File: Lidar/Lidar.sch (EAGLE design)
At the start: 4 parts

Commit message: board schematic
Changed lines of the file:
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@@
 <grid distance="0.1" unitdist="inch" unit="inch" style="lines" multiple="1" display="no" altdistance="0.01" altunitdist="inch" altunit="inch"/>
 <layers>
-<layer number="1" name="Top" color="4" fill="1" visible="yes" active="no"/>
-<layer number="16" name="Bottom" color="1" fill="1" visible="yes" active="no"/>
-<layer number="17" name="Pads" color="2" fill="1" visible="yes" active="no"/>
-<layer number="18" name="Vias" color="2" fill="1" visible="yes" active="no"/>
-<layer number="19" name="Unrouted" color="6" fill="1" visible="yes" active="no"/>
-<layer number="20" name="Dimension" color="15" fill="1" visible="yes" active="no"/>
-<layer number="21" name="tPlace" color="7" fill="1" visible="yes" active="no"/>
-<layer number="22" name="bPlace" color="7" fill="1" visible="yes" active="no"/>
-<layer number="23" name="tOrigins" color="15" fill="1" visible="yes" active="no"/>
-<layer number="24" name="bOrigins" color="15" fill="1" visible="yes" active="no"/>
-<layer number="25" name="tNames" color="7" fill="1" visible="yes" active="no"/>
-<layer number="26" name="bNames" color="7" fill="1" visible="yes" active="no"/>
-<layer number="27" name="tValues" color="7" fill="1" visible="yes" active="no"/>
-<layer number="28" name="bValues" color="7" fill="1" visible="yes" active="no"/>
+<layer number="1" name="Top" color="4" fill="1" visible="no" active="no"/>
+<layer number="16" name="Bottom" color="1" fill="1" visible="no" active="no"/>
+<layer number="17" name="Pads" color="2" fill="1" visible="no" active="no"/>
+<layer number="18" name="Vias" color="2" fill="1" visible="no" active="no"/>
+<layer number="19" name="Unrouted" color="6" fill="1" visible="no" active="no"/>
+<layer number="20" name="Dimension" color="15" fill="1" visible="no" active="no"/>
+<layer number="21" name="tPlace" color="7" fill="1" visible="no" active="no"/>
+<layer number="22" name="bPlace" color="7" fill="1" visible="no" active="no"/>
+<layer number="23" name="tOrigins" color="15" fill="1" visible="no" active="no"/>
+<layer number="24" name="bOrigins" color="15" fill="1" visible="no" active="no"/>
+<layer number="25" name="tNames" color="7" fill="1" visible="no" active="no"/>
+<layer number="26" name="bNames" color="7" fill="1" visible="no" active="no"/>
+<layer number="27" name="tValues" color="7" fill="1" visible="no" active="no"/>
+<layer number="28" name="bValues" color="7" fill="1" visible="no" active="no"/>
 <layer number="29" name="tStop" color="7" fill="3" visible="no" active="no"/>
 <layer number="30" name="bStop" color="7" fill="6" visible="no" active="no"/>
@@
 <layer number="35" name="tGlue" color="7" fill="4" visible="no" active="no"/>
 <layer number="36" name="bGlue" color="7" fill="5" visible="no" active="no"/>
-<layer number="37" name="tTest" color="7" fill="1" visible="yes" active="no"/>
-<layer number="38" name="bTest" color="7" fill="1" visible="yes" active="no"/>
+<layer number="37" name="tTest" color="7" fill="1" visible="no" active="no"/>
+<layer number="38" name="bTest" color="7" fill="1" visible="no" active="no"/>
 <layer number="39" name="tKeepout" color="4" fill="11" visible="no" active="no"/>
 <layer number="40" name="bKeepout" color="1" fill="11" visible="no" active="no"/>
@@
 <layer number="44" name="Drills" color="7" fill="1" visible="no" active="no"/>
 <layer number="45" name="Holes" color="7" fill="1" visible="no" active="no"/>
-<layer number="46" name="Milling" color="3" fill="1" visible="yes" active="no"/>
-<layer number="47" name="Measures" color="7" fill="1" visible="yes" active="no"/>
-<layer number="48" name="Document" color="7" fill="1" visible="yes" active="no"/>
-<layer number="49" name="Reference" color="7" fill="1" visible="yes" active="no"/>
-<layer number="50" name="dxf" color="7" fill="1" visible="yes" active="no"/>
-<layer number="51" name="tDocu" color="7" fill="1" visible="yes" active="no"/>
-<layer number="52" name="bDocu" color="7" fill="1" visible="yes" active="no"/>
-<layer number="53" name="tGND_GNDA" color="7" fill="9" visible="yes" active="no"/>
-<layer number="54" name="bGND_GNDA" color="1" fill="9" visible="yes" active="no"/>
-<layer number="56" name="wert" color="7" fill="1" visible="yes" active="no"/>
-<layer number="57" name="tCAD" color="7" fill="1" visible="yes" active="no"/>
-<layer number="58" name="bCAD" color="7" fill="1" visible="yes" active="no"/>
-<layer number="59" name="tCarbon" color="7" fill="1" visible="yes" active="no"/>
-<layer number="60" name="bCarbon" color="7" fill="1" visible="yes" active="no"/>
+<layer number="46" name="Milling" color="3" fill="1" visible="no" active="no"/>
+<layer number="47" name="Measures" color="7" fill="1" visible="no" active="no"/>
+<layer number="48" name="Document" color="7" fill="1" visible="no" active="no"/>
+<layer number="49" name="Reference" color="7" fill="1" visible="no" active="no"/>
+<layer number="50" name="dxf" color="7" fill="1" visible="no" active="no"/>
+<layer number="51" name="tDocu" color="7" fill="1" visible="no" active="no"/>
+<layer number="52" name="bDocu" color="7" fill="1" visible="no" active="no"/>
+<layer number="53" name="tGND_GNDA" color="7" fill="9" visible="no" active="no"/>
+<layer number="54" name="bGND_GNDA" color="1" fill="9" visible="no" active="no"/>
+<layer number="56" name="wert" color="7" fill="1" visible="no" active="no"/>
+<layer number="57" name="tCAD" color="7" fill="1" visible="no" active="no"/>
+<layer number="58" name="bCAD" color="7" fill="1" visible="no" active="no"/>
+<layer number="59" name="tCarbon" color="7" fill="1" visible="no" active="no"/>
+<layer number="60" name="bCarbon" color="7" fill="1" visible="no" active="no"/>
 <layer number="88" name="SimResults" color="9" fill="1" visible="yes" active="yes"/>
 <layer number="89" name="SimProbes" color="9" fill="1" visible="yes" active="yes"/>
@@
 </variantdefs>
 <classes>
-<class number="0" name="default" width="0" drill="0">
+<class number="0" name="default" width="0.8128" drill="0.1016">
+<clearance class="0" value="0.1016"/>
 </class>
 </classes>
@@
 <part name="CONN-LIDAR" library="SparkFun-Connectors" library_urn="urn:adsk.eagle:library:513" deviceset="CONN_05" device="PTH" package3d_urn="urn:adsk.eagle:package:38104/2"/>
 <part name="ESP32" library="ESP32-DEVKITC-32D" deviceset="ESP32-DEVKITC-32D" device=""/>
+<part name="GND1" library="supply1" library_urn="urn:adsk.eagle:library:371" deviceset="GND" device=""/>
 </parts>
 <sheets>
@@
 <attribute name="NAME" x="48.2428" y="104.8043" size="1.78" layer="95"/>
 <attribute name="VALUE" x="48.2437" y="50.7702" size="1.7799" layer="96"/>
+</instance>
+<instance part="GND1" gate="1" x="111.76" y="116.84" smashed="yes" rot="R180">
+<attribute name="VALUE" x="114.3" y="119.38" size="1.778" layer="96" rot="R180"/>
 </instance>
 </instances>
@@
 <label x="114.3" y="104.14" size="1.778" layer="95"/>
 <label x="86.36" y="101.6" size="1.778" layer="95"/>
-</segment>
-</net>
+<pinref part="GND1" gate="1" pin="GND"/>
+<wire x1="111.76" y1="101.6" x2="111.76" y2="114.3" width="0.1524" layer="91"/>
+</segment>
+</net>

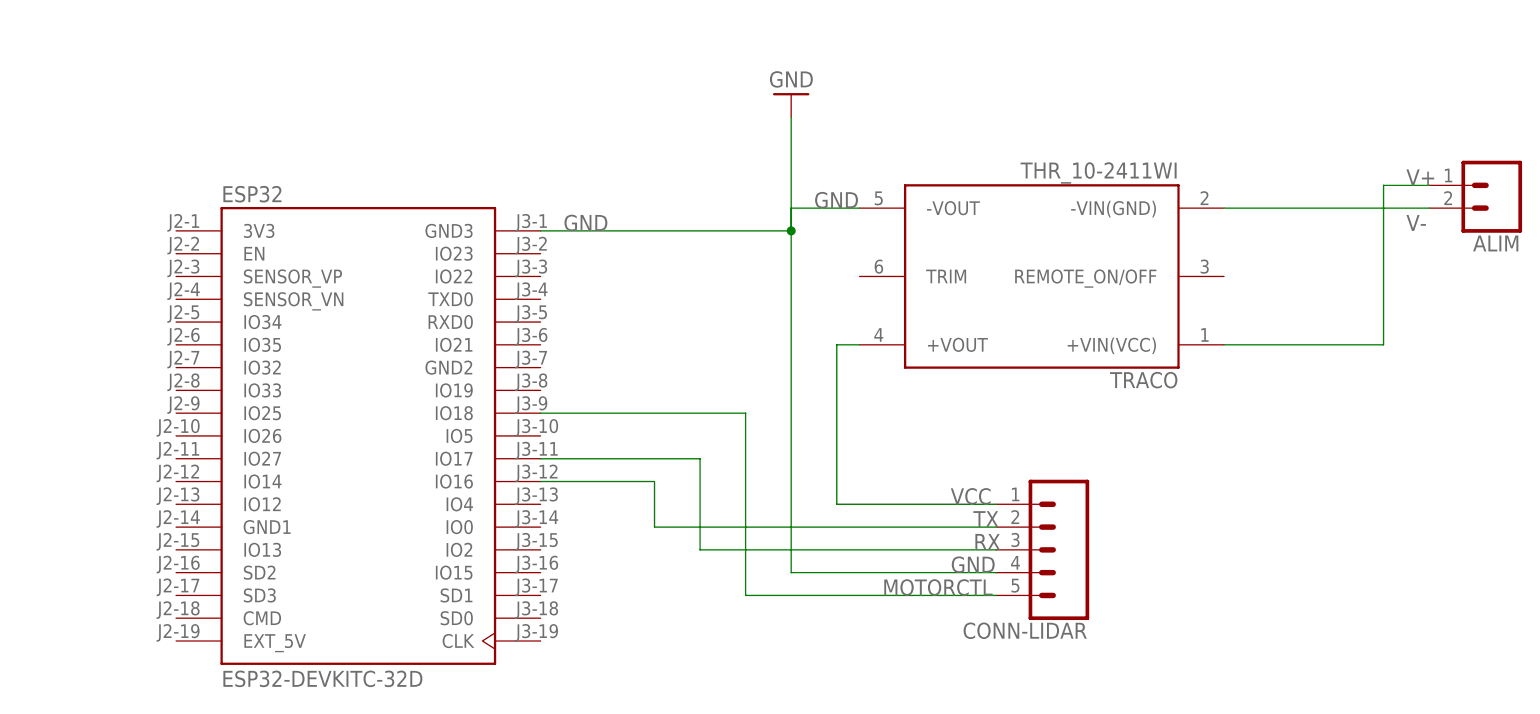
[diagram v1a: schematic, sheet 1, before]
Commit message: add(lidar): POWER LED + reduce the board size
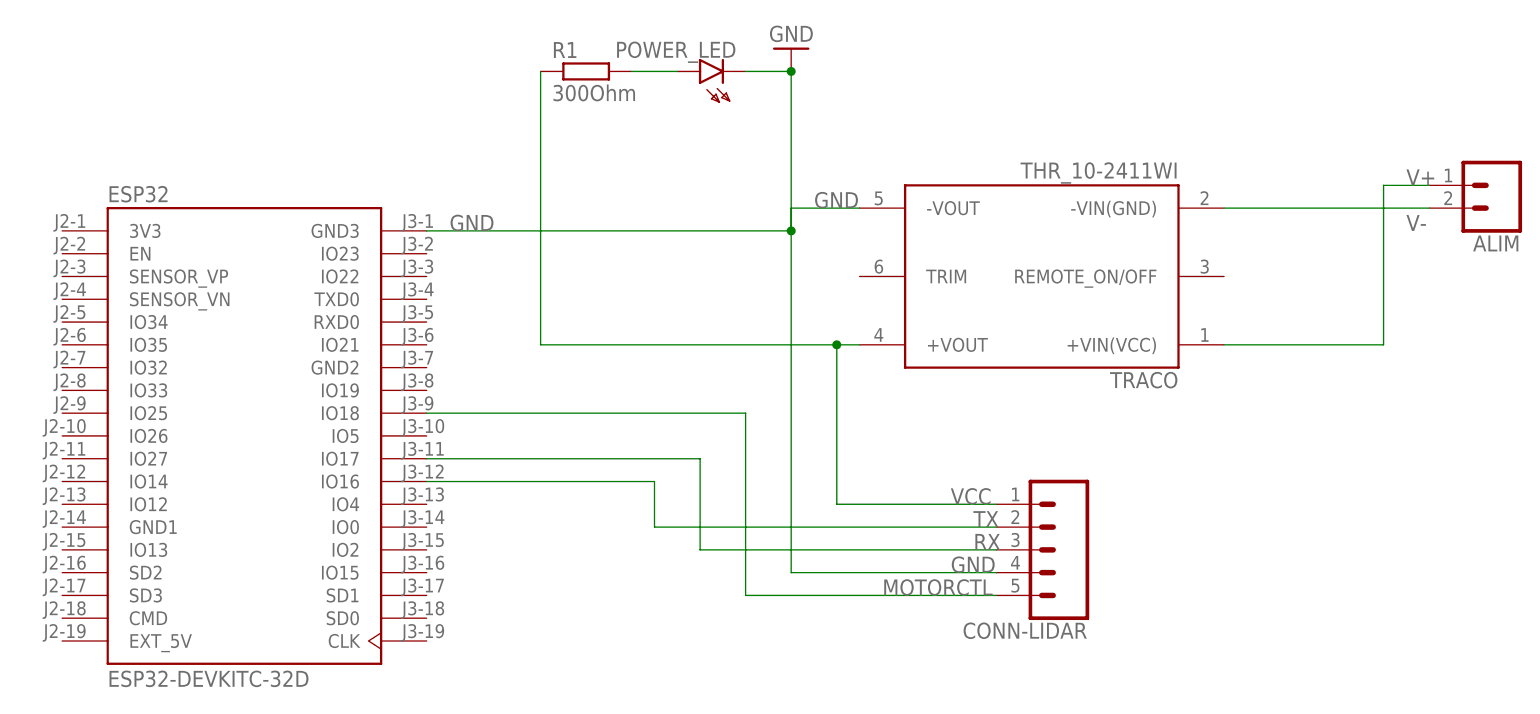
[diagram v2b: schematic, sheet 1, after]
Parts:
- added POWER_LED: HLMP6, display-hp:HLMP6
- added R1: 300Ohm, rcl:R-EU_0411/15
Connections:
- new net N$1: POWER_LED.A, R1.2
- net GND: now also POWER_LED.K
- net VCC: now also R1.1
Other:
- moved on the sheet: ESP32
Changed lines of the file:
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@@
 <part name="ESP32" library="ESP32-DEVKITC-32D" deviceset="ESP32-DEVKITC-32D" device=""/>
 <part name="GND1" library="supply1" library_urn="urn:adsk.eagle:library:371" deviceset="GND" device=""/>
+<part name="POWER_LED" library="display-hp" library_urn="urn:adsk.eagle:library:212" deviceset="HLMP6" device="" package3d_urn="urn:adsk.eagle:package:12992/1"/>
+<part name="R1" library="rcl" library_urn="urn:adsk.eagle:library:334" deviceset="R-EU_" device="0411/15" package3d_urn="urn:adsk.eagle:package:23568/2" value="300Ohm"/>
 </parts>
 <sheets>
@@
 <attribute name="NAME" x="144.78" y="57.912" size="1.778" layer="95" font="vector" rot="R180"/>
 </instance>
-<instance part="ESP32" gate="G$1" x="63.5" y="78.74" smashed="yes">
-<attribute name="NAME" x="48.2428" y="104.8043" size="1.78" layer="95"/>
-<attribute name="VALUE" x="48.2437" y="50.7702" size="1.7799" layer="96"/>
+<instance part="ESP32" gate="G$1" x="50.8" y="78.74" smashed="yes">
+<attribute name="NAME" x="35.5428" y="104.8043" size="1.78" layer="95"/>
+<attribute name="VALUE" x="35.5437" y="50.7702" size="1.7799" layer="96"/>
 </instance>
-<instance part="GND1" gate="1" x="111.76" y="116.84" smashed="yes" rot="R180">
-<attribute name="VALUE" x="114.3" y="119.38" size="1.778" layer="96" rot="R180"/>
+<instance part="GND1" gate="1" x="111.76" y="121.92" smashed="yes" rot="R180">
+<attribute name="VALUE" x="114.3" y="124.46" size="1.778" layer="96" rot="R180"/>
+</instance>
+<instance part="POWER_LED" gate="A" x="104.14" y="119.38" smashed="yes" rot="R90">
+<attribute name="NAME" x="105.664" y="122.682" size="1.778" layer="95" rot="R180"/>
+</instance>
+<instance part="R1" gate="G$1" x="88.9" y="119.38" smashed="yes">
+<attribute name="NAME" x="85.09" y="120.8786" size="1.778" layer="95"/>
+<attribute name="VALUE" x="85.09" y="116.078" size="1.778" layer="96"/>
 </instance>
 </instances>
@@
 <segment>
 <pinref part="ESP32" gate="G$1" pin="IO16"/>
-<wire x1="83.82" y1="73.66" x2="96.52" y2="73.66" width="0.1524" layer="91"/>
+<wire x1="71.12" y1="73.66" x2="96.52" y2="73.66" width="0.1524" layer="91"/>
 <pinref part="CONN-LIDAR" gate="J1" pin="2"/>
 <wire x1="96.52" y1="73.66" x2="96.52" y2="68.58" width="0.1524" layer="91"/>
@@
 <segment>
 <pinref part="ESP32" gate="G$1" pin="IO18"/>
-<wire x1="83.82" y1="81.28" x2="106.68" y2="81.28" width="0.1524" layer="91"/>
+<wire x1="71.12" y1="81.28" x2="106.68" y2="81.28" width="0.1524" layer="91"/>
 <wire x1="106.68" y1="81.28" x2="106.68" y2="60.96" width="0.1524" layer="91"/>
 <pinref part="CONN-LIDAR" gate="J1" pin="5"/>
@@
 <wire x1="119.38" y1="104.14" x2="111.76" y2="104.14" width="0.1524" layer="91"/>
 <pinref part="ESP32" gate="G$1" pin="GND3"/>
-<wire x1="83.82" y1="101.6" x2="111.76" y2="101.6" width="0.1524" layer="91"/>
+<wire x1="71.12" y1="101.6" x2="111.76" y2="101.6" width="0.1524" layer="91"/>
 <junction x="111.76" y="101.6"/>
 <label x="129.54" y="63.5" size="1.778" layer="95"/>
 <label x="114.3" y="104.14" size="1.778" layer="95"/>
-<label x="86.36" y="101.6" size="1.778" layer="95"/>
+<label x="73.66" y="101.6" size="1.778" layer="95"/>
 <pinref part="GND1" gate="1" pin="GND"/>
-<wire x1="111.76" y1="101.6" x2="111.76" y2="114.3" width="0.1524" layer="91"/>
+<wire x1="111.76" y1="101.6" x2="111.76" y2="119.38" width="0.1524" layer="91"/>
+<pinref part="POWER_LED" gate="A" pin="K"/>
+<wire x1="106.68" y1="119.38" x2="111.76" y2="119.38" width="0.1524" layer="91"/>
+<junction x="111.76" y="119.38"/>
 </segment>
 </net>
@@
 <wire x1="116.84" y1="88.9" x2="119.38" y2="88.9" width="0.1524" layer="91"/>
 <label x="129.54" y="71.12" size="1.778" layer="95"/>
+<wire x1="116.84" y1="88.9" x2="83.82" y2="88.9" width="0.1524" layer="91"/>
+<junction x="116.84" y="88.9"/>
+<wire x1="83.82" y1="88.9" x2="83.82" y2="119.38" width="0.1524" layer="91"/>
+<pinref part="R1" gate="G$1" pin="1"/>
 </segment>
 </net>
@@
 <label x="132.08" y="66.04" size="1.778" layer="95"/>
 <pinref part="ESP32" gate="G$1" pin="IO17"/>
-<wire x1="101.6" y1="76.2" x2="83.82" y2="76.2" width="0.1524" layer="91"/>
+<wire x1="101.6" y1="76.2" x2="71.12" y2="76.2" width="0.1524" layer="91"/>
+</segment>
+</net>
+<net name="N$1" class="0">
+<segment>
+<pinref part="R1" gate="G$1" pin="2"/>
+<pinref part="POWER_LED" gate="A" pin="A"/>
+<wire x1="93.98" y1="119.38" x2="99.06" y2="119.38" width="0.1524" layer="91"/>
 </segment>
 </net>
@@
 packages will not be understood (or retained) with this version.
 </note>
+<note version="8.4" severity="warning">
+Since Version 8.4, EAGLE supports properties for SPICE simulation.
+Probes in schematics and SPICE mapping objects found in parts and library devices
+will not be understood with this version. Update EAGLE to the latest version
+for full support of SPICE simulation.
+</note>
 </compatibility>
